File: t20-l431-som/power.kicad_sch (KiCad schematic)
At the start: 42 parts, among them U1 STM32L431-WLCSP64, U2 T20W80, U4 MODULE_INTERNAL_T20_L431_HOST, U5 LP3986TL-2518/NOPB, U7 TPS22916BYFPR, U9 NCP139AFCT120T2G

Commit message: Various layout fixes for DRC
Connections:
- net 1V8: now also U4.D11 (1V8), U4.E10 (1V8)
- net GND: now also U4.E11 (GND)

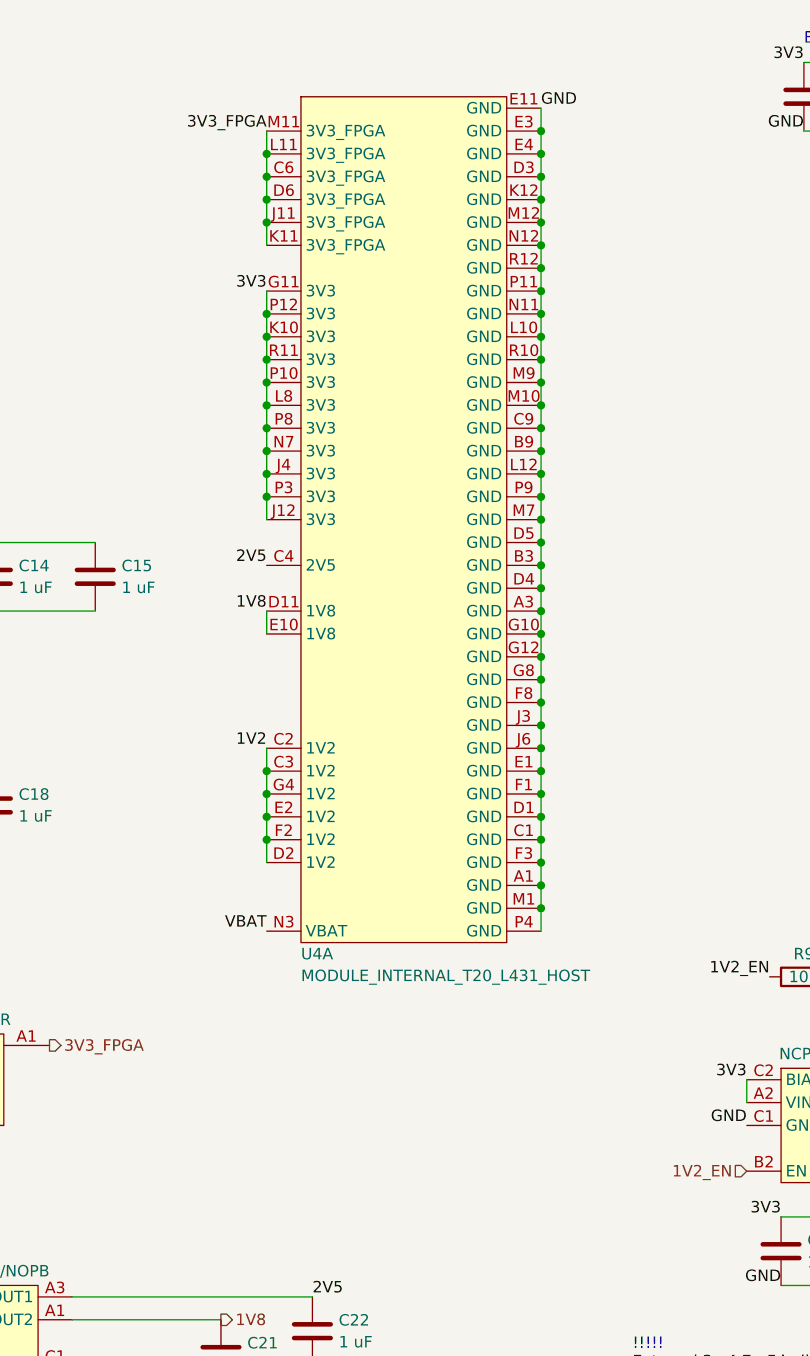
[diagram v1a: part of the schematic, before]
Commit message: T20/L431 SoM: added power/ground connections to all remaining NC lands
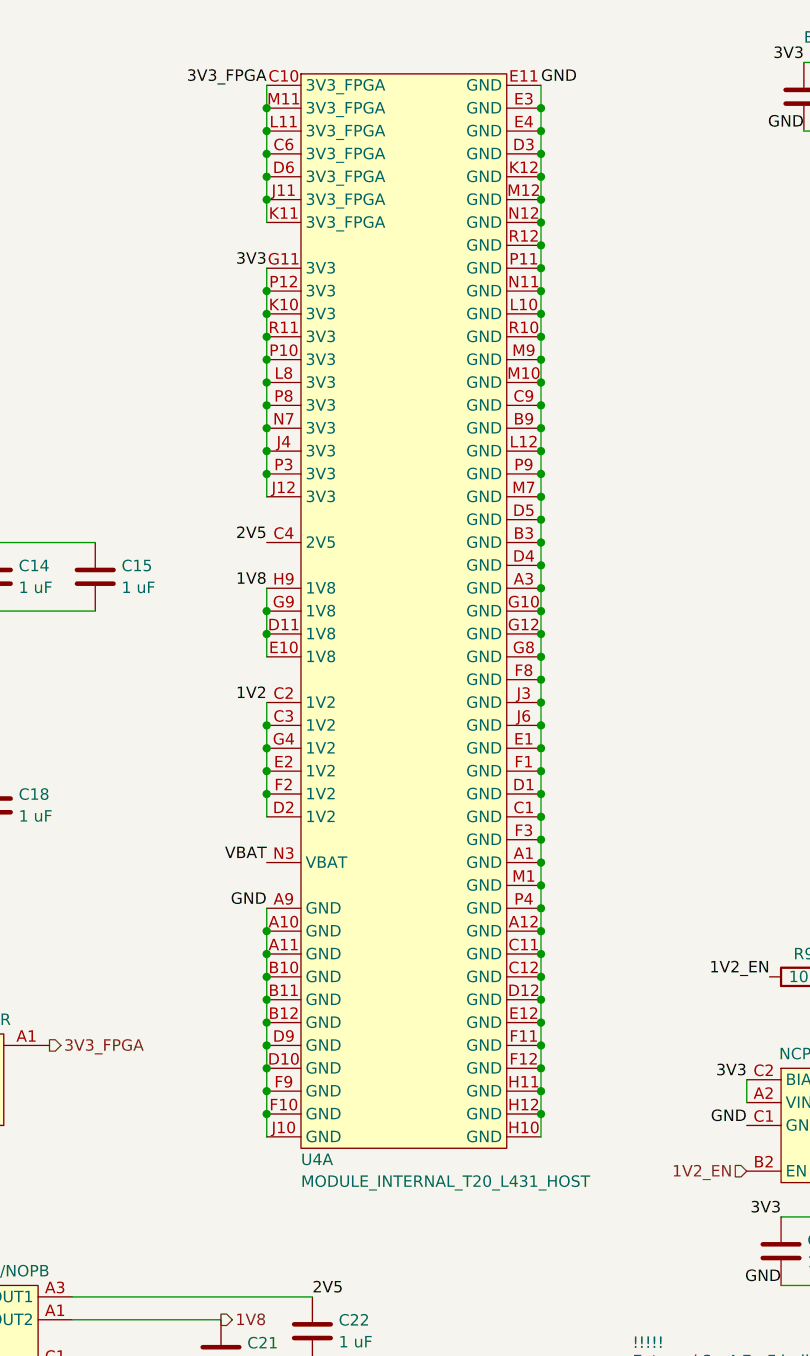
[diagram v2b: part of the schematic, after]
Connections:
- net 1V8: now also U4.G9 (1V8), U4.H9 (1V8)
- net 3V3_FPGA: now also U4.C10 (3V3_FPGA)
- net GND: now also U4.A10 (GND), U4.A11 (GND), U4.A12 (GND), U4.A9 (GND), U4.B10 (GND), U4.B11 (GND), U4.B12 (GND), U4.C11 (GND), U4.C12 (GND), U4.D10 (GND), U4.D12 (GND), U4.D9 (GND), U4.E12 (GND), U4.F10 (GND), U4.F11 (GND), U4.F12 (GND), U4.F9 (GND), U4.H10 (GND), U4.H11 (GND), U4.H12 (GND), U4.J10 (GND)
